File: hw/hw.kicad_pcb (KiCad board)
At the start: 2 copper layers, 99.1 x 99.1 mm, 45 parts, among them J1 Keyboard, J2 CPU1, J3 ISP, J4 UART, J5 A[0..15], J7 D[0..7], J8 VGA, M1 MOUNT, M2 MOUNT, M3 MOUNT, M4 MOUNT, U1 ATmega328P-PU, U10 CY7C199, U11 74LS04, U12 74LS165, U2 74LS161, U3 74LS74, U4 74LS08, U5 74LS138, U6 Z80CPU, U7 74LS299, U8 74LS32, U9 74LS74, X1 CXO_DIP8

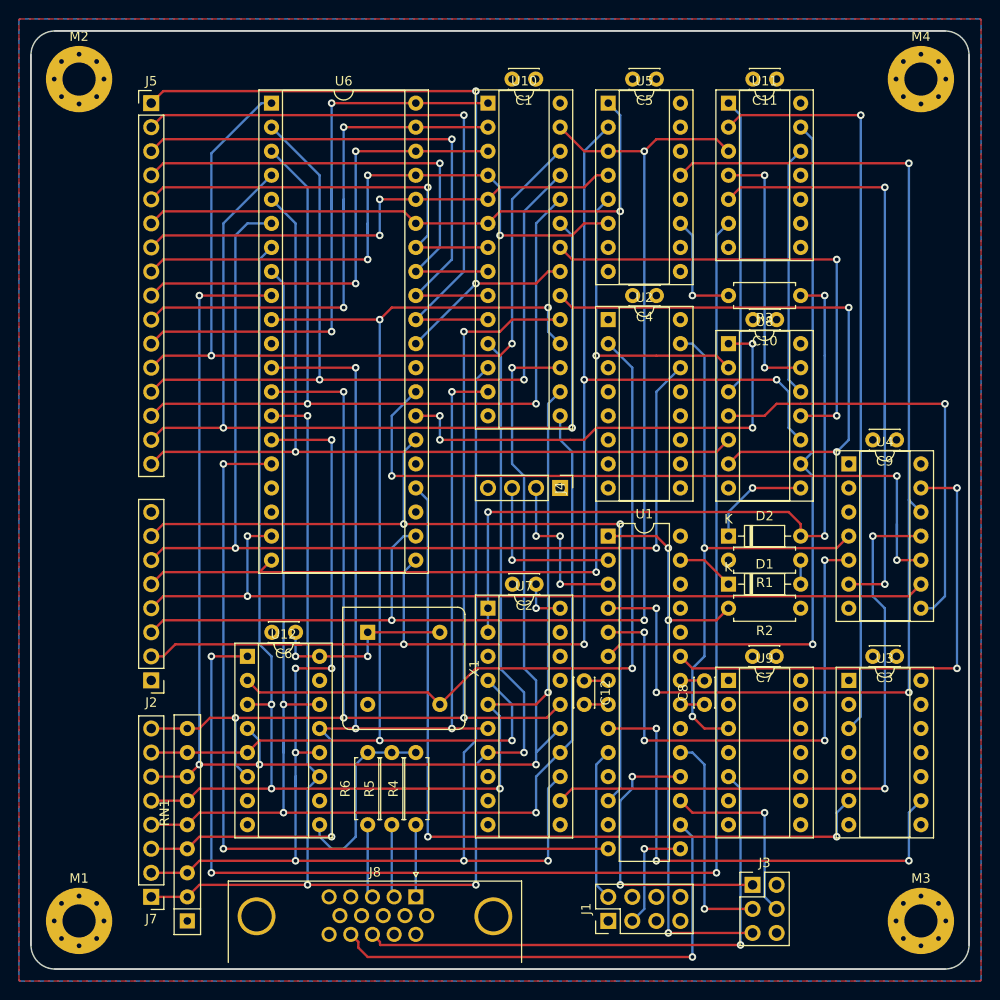
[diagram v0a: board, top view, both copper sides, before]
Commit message: PCB now fully connected
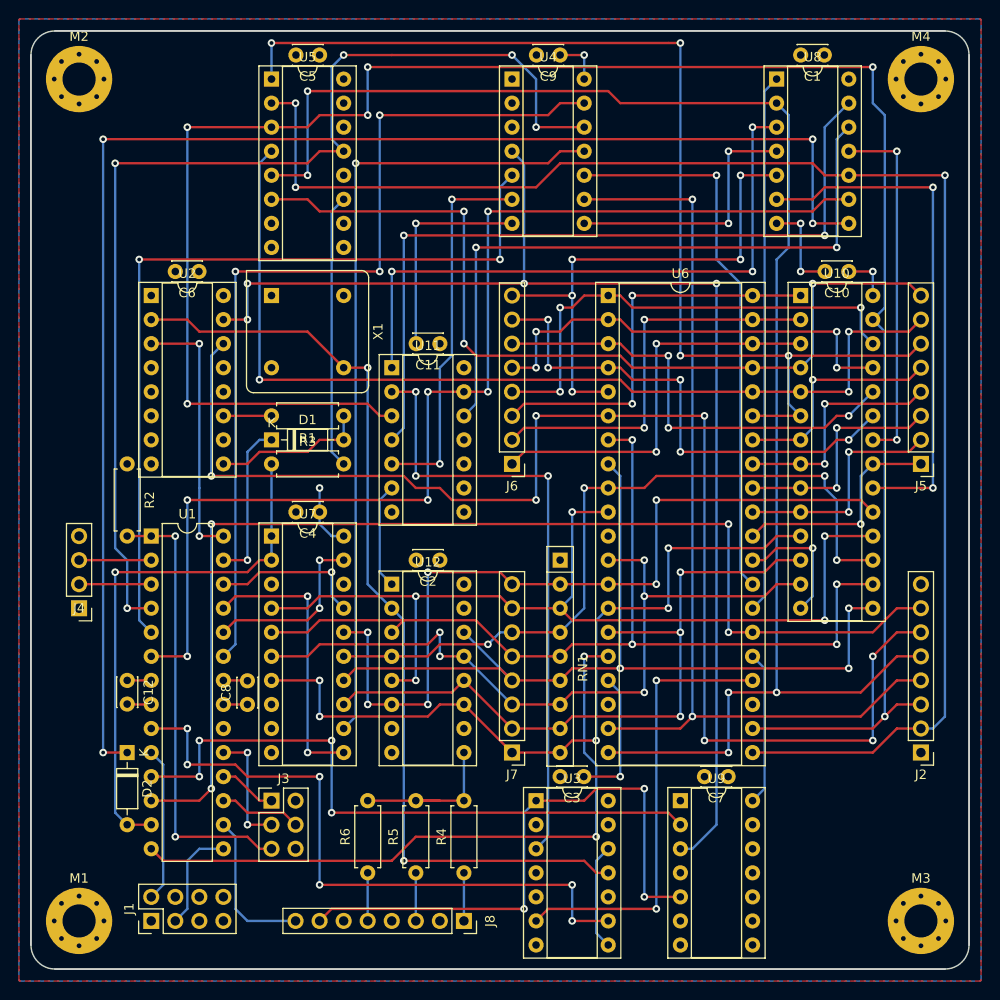
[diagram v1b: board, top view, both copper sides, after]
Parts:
- added J6: A[8..15], Connector_PinHeader_2.54mm:PinHeader_1x08_P2.54mm_Vertical, F.Cu at (127.0, 96.5)
- J5: value A[0..15] -> A[0..7]; footprint Connector_PinHeader_2.54mm:PinHeader_1x16_P2.54mm_Vertical -> Connector_PinHeader_2.54mm:PinHeader_1x08_P2.54mm_Vertical
- J8: footprint Connector_Dsub:DSUB-15-HD_Female_Horizontal_P2.29x1.98mm_EdgePinOffset3.03mm_Housed_MountingHolesOffset4.94mm -> Connector_PinSocket_2.54mm:PinSocket_1x08_P2.54mm_Vertical
- RN1: value 1K -> R_Network08_US
- moved J5 89.8 mm to (170.2, 96.5), turned to 180 degrees
- moved J2 81.6 mm to (170.2, 127.0)
- moved R2 72.7 mm to (86.4, 96.5), turned to 270 degrees
- moved D2 67.5 mm to (86.4, 127.0), turned to 270 degrees
- moved R3 58.6 mm to (101.6, 96.5), turned to 0 degrees
- moved RN1 54.8 mm to (132.1, 106.7), turned to 270 degrees
- moved U4 54.0 mm to (127.0, 55.9)
- moved C9 54.0 mm to (132.1, 53.3)
- moved J4 52.4 mm to (81.3, 111.8), turned to 180 degrees
- moved J3 51.6 mm to (101.6, 132.1)
- moved D1 50.6 mm to (101.6, 94.0)
- moved R1 50.6 mm to (109.2, 91.4)
- moved U2 48.3 mm to (88.9, 78.7)
- moved C12 48.3 mm to (86.4, 119.4)
- moved C8 48.3 mm to (99.1, 121.9)
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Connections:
- J8 pad 2: Net-(J8-Pad2) -> GND
- J8 pad 4: (no net) -> GND
- J8 pad 5: GND -> Net-(J8-Pad5)
- J8 pad 7: GND -> /HSYNC
- J8 pad 8: GND -> /VSYNC
- R5 pad 1: Net-(J8-Pad2) -> Net-(J8-Pad3)
- R6 pad 1: Net-(J8-Pad3) -> Net-(J8-Pad5)
- RN1 pad 2: /D0 -> /D7
- RN1 pad 3: /D1 -> /D6
- RN1 pad 4: /D2 -> /D5
- RN1 pad 5: /D3 -> /D4
- RN1 pad 6: /D4 -> /D3
- RN1 pad 7: /D5 -> /D2
- RN1 pad 8: /D6 -> /D1
- RN1 pad 9: /D7 -> /D0
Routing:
- net Net-(D2-Pad1): track 11.2 -> 154.9 mm, vias 1 -> 4
- net /~DPY_PL: track 149.1 -> 11.2 mm, vias 3 -> 0
- net /D1: track 163.4 -> 75.3 mm, vias 7 -> 3
- net /~WR: track 132.7 -> 218.3 mm, vias 3 -> 6
- net /D5: track 154.3 -> 79.4 mm, vias 5 -> 4
- net /CHAR_TC: track 61.8 -> 132.4 mm, vias 2 -> 4
- net /D0: track 152.3 -> 82.9 mm, vias 4 -> 5
- net /HSYNC_RAW: track 0.00 -> 67.8 mm, vias 0 -> 4
- net /~IO_REQ: track 103.7 -> 167.0 mm, vias 2 -> 5
- net /D7: track 144.5 -> 87.4 mm, vias 5 -> 6
- net /D2: track 135.7 -> 80.4 mm
- net /D3: track 147.9 -> 93.1 mm
- net /A5: track 63.1 -> 117.9 mm, vias 1 -> 4
- net Net-(U11-Pad4): track 27.9 -> 81.6 mm
- net /A0: track 73.5 -> 23.9 mm, vias 2 -> 1
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
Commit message: generate PCB output
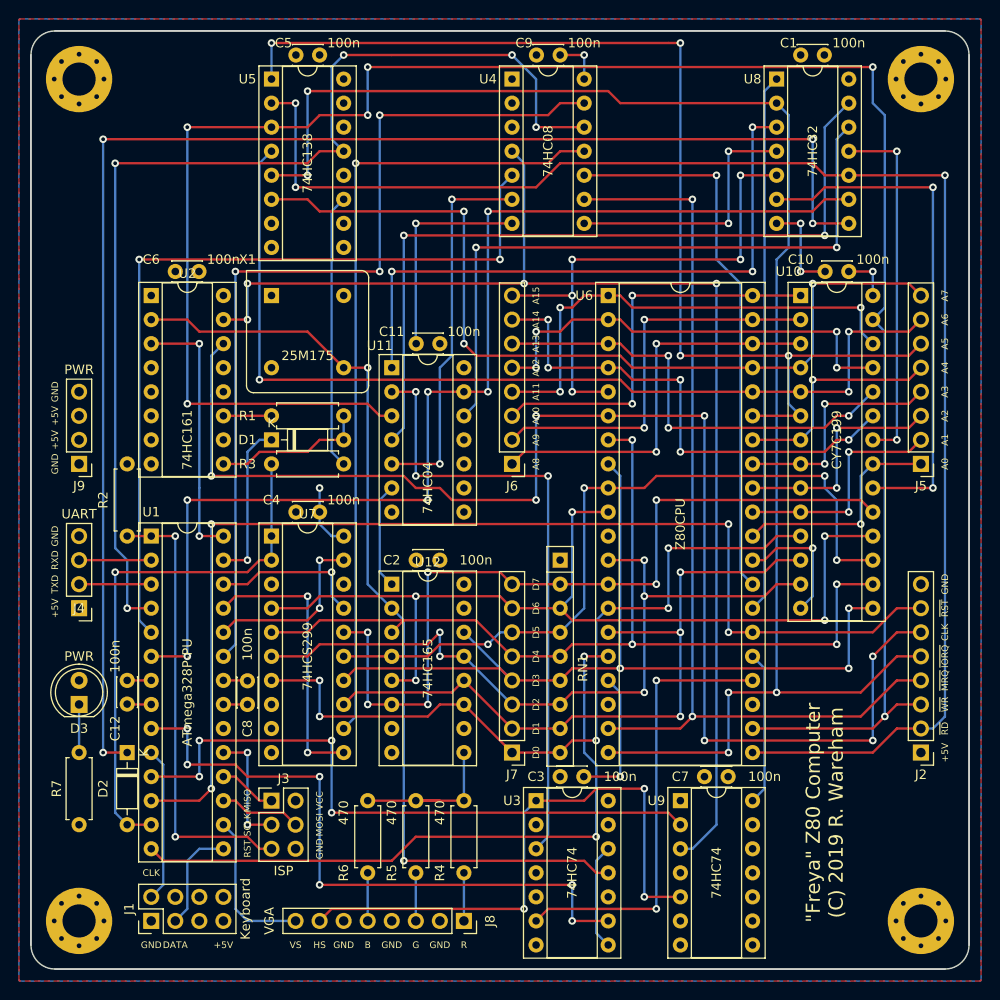
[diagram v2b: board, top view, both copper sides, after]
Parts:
- added D3: PWR, LED_THT:LED_D5.0mm, F.Cu at (81.3, 121.9)
- added J9: PWR, Connector_PinHeader_2.54mm:PinHeader_1x04_P2.54mm_Vertical, F.Cu at (81.3, 96.5)
- added R7: 220, Resistor_THT:R_Axial_DIN0207_L6.3mm_D2.5mm_P7.62mm_Horizontal, F.Cu at (81.3, 134.6)
- J2: value CPU1 -> CPU
- RN1: value R_Network08_US -> 220R
- U1: footprint Package_DIP:DIP-28_W7.62mm -> Package_DIP:DIP-28_W7.62mm_Socket
- U11: value 74LS04 -> 74HC04
- U12: value 74LS165 -> 74HC165
- U2: value 74LS161 -> 74HC161
- U3, U9: value 74LS74 -> 74HC74
- U4: value 74LS08 -> 74HC08
- U5: value 74LS138 -> 74HC138
- U7: value 74LS299 -> 74HCS299
- U8: value 74LS32 -> 74HC32
- X1: value CXO_DIP8 -> 25M175
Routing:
- net Net-(D3-Pad1): track 0.00 -> 5.08 mm
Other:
- board text added: ""Freya" Z80 Computer (C) 2019 R. Wareham"
- board text added: "+5V"
- board text added: "A0"
- board text added: "A1"
- board text added: "A10"
- board text added: "A11"
- board text added: "A12"
- board text added: "A13"
- board text added: "A14"
- board text added: "A15"
- board text added: "A2"
- board text added: "A3"
- board text added: "A4"
- board text added: "A5"
- board text added: "A6"
- board text added: "A7"
- board text added: "A8"
- board text added: "A9"
- board text added: "B"
- board text added: "CLK"
- board text added: "D0"
- board text added: "D1"
- board text added: "D2"
- board text added: "D3"
- board text added: "D4"
- board text added: "D5"
- board text added: "D6"
- board text added: "D7"
- board text added: "DATA"
- board text added: "G"
- board text added: "GND"
- board text added: "HS"
- board text added: "MISO"
- board text added: "MOSI"
- board text added: "R"
- board text added: "RST"
- board text added: "RXD"
- board text added: "SCLK"
- board text added: "TXD"
- board text added: "VCC"
- board text added: "VS"
- board text added: "~IORQ"
- board text added: "~MRQ"
- board text added: "~RD"
- board text added: "~RST"
- board text added: "~WR"
